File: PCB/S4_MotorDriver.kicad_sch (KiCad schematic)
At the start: 24 parts, among them J1 Motor Out, J2 ESTOP, U1 DRV8873SPWPRQ1

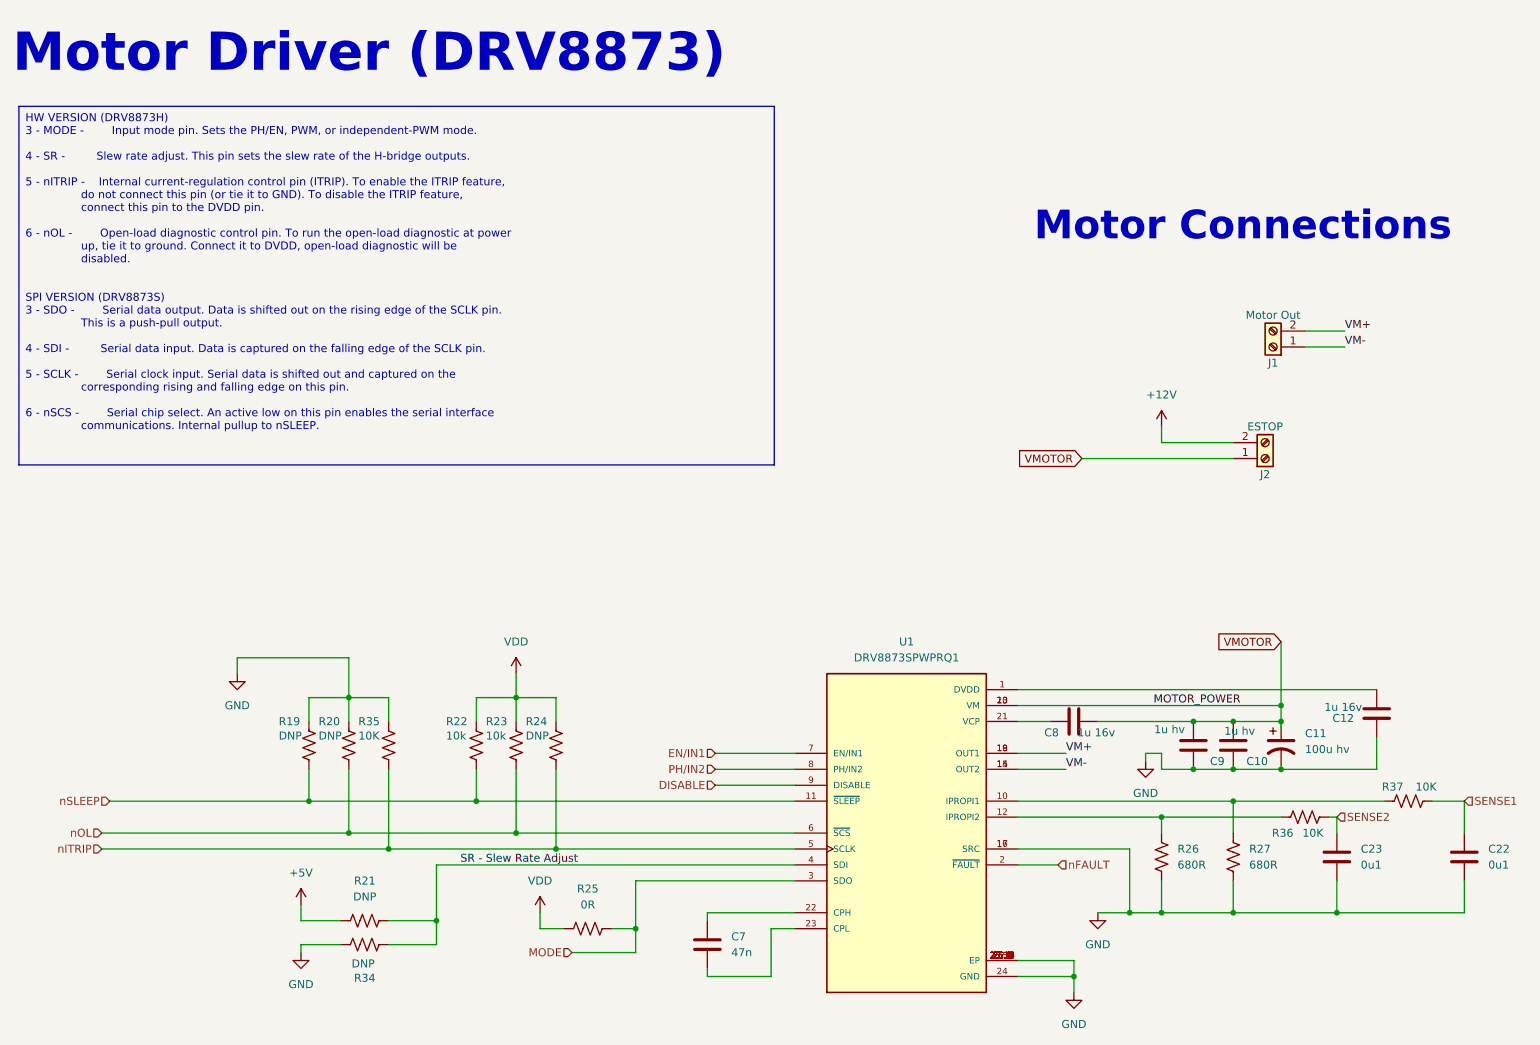
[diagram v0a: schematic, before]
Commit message: Update PCB to seperate ground symbols apporiately. Modify board to sepearte ground path for motor current and all other devices. Add filtering for slide power, hopefully reduce bownout or other issue.
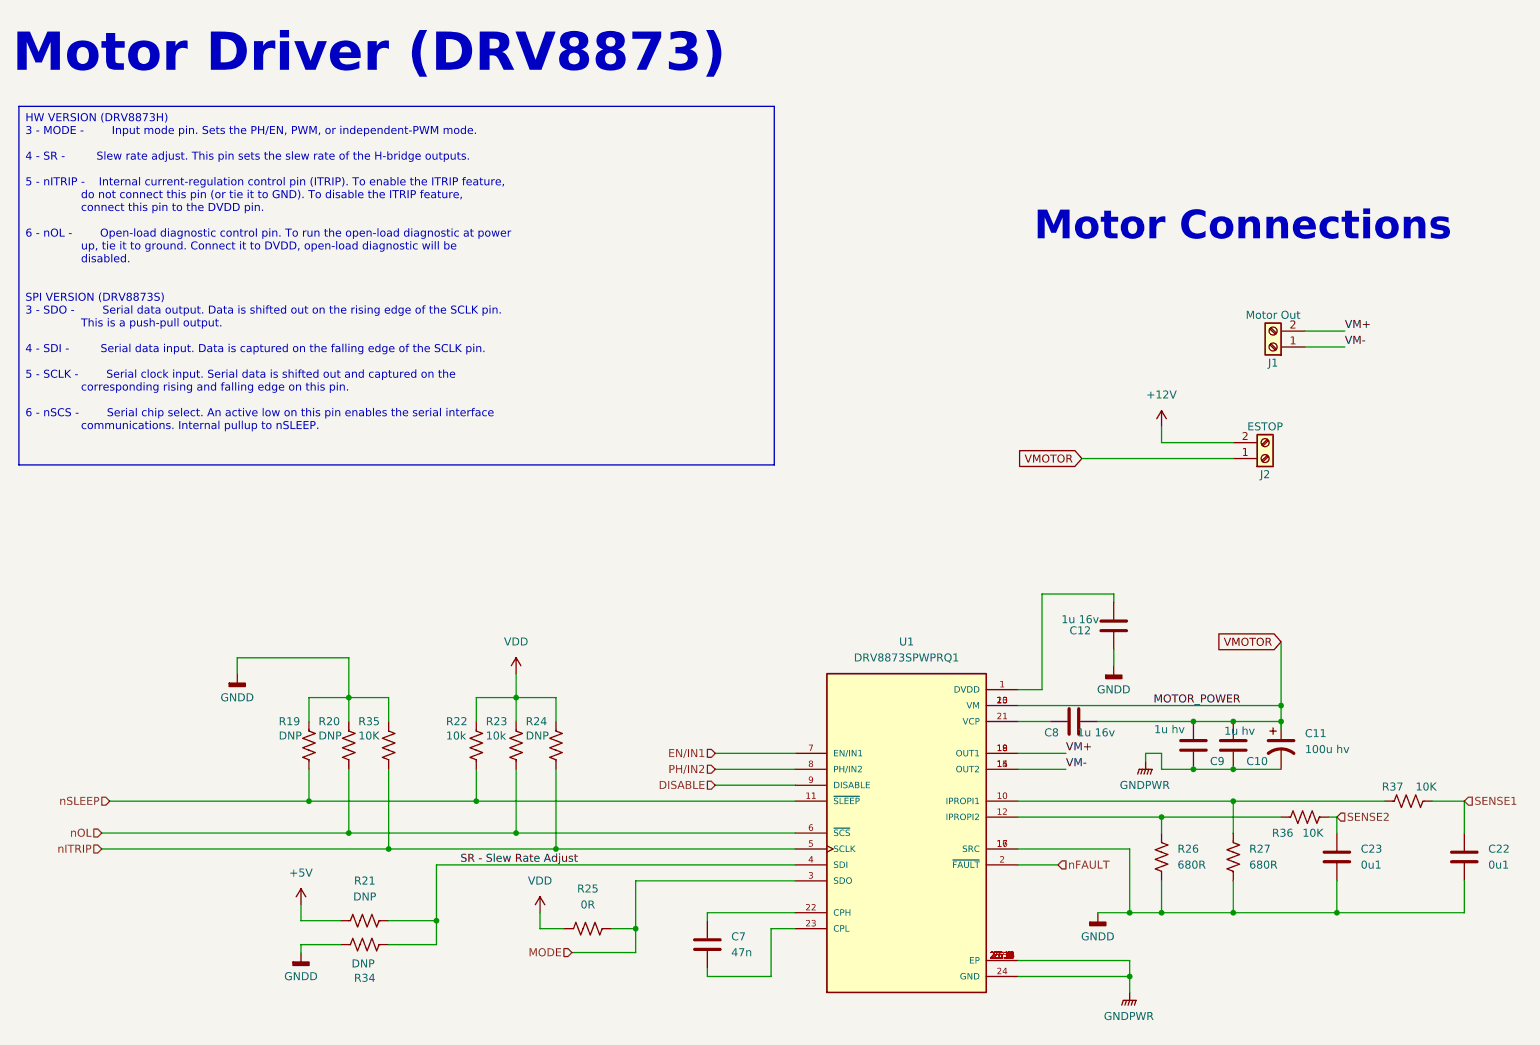
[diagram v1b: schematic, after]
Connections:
- net GND renamed GNDPWR
- net GNDPWR: no longer C12.2, C22.2, C23.2, R19.2, R20.2, R26.1, R27.1, R34.1, R35.2, U1.16 (SRC), U1.17 (SRC)
- new net GNDD: C12.2, C22.2, C23.2, R19.2, R20.2, R26.1, R27.1, R34.1, R35.2, U1.16 (SRC), U1.17 (SRC)
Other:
- moved on the sheet: C12

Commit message: WIP Adding adudino onboard, so far copying pro mega
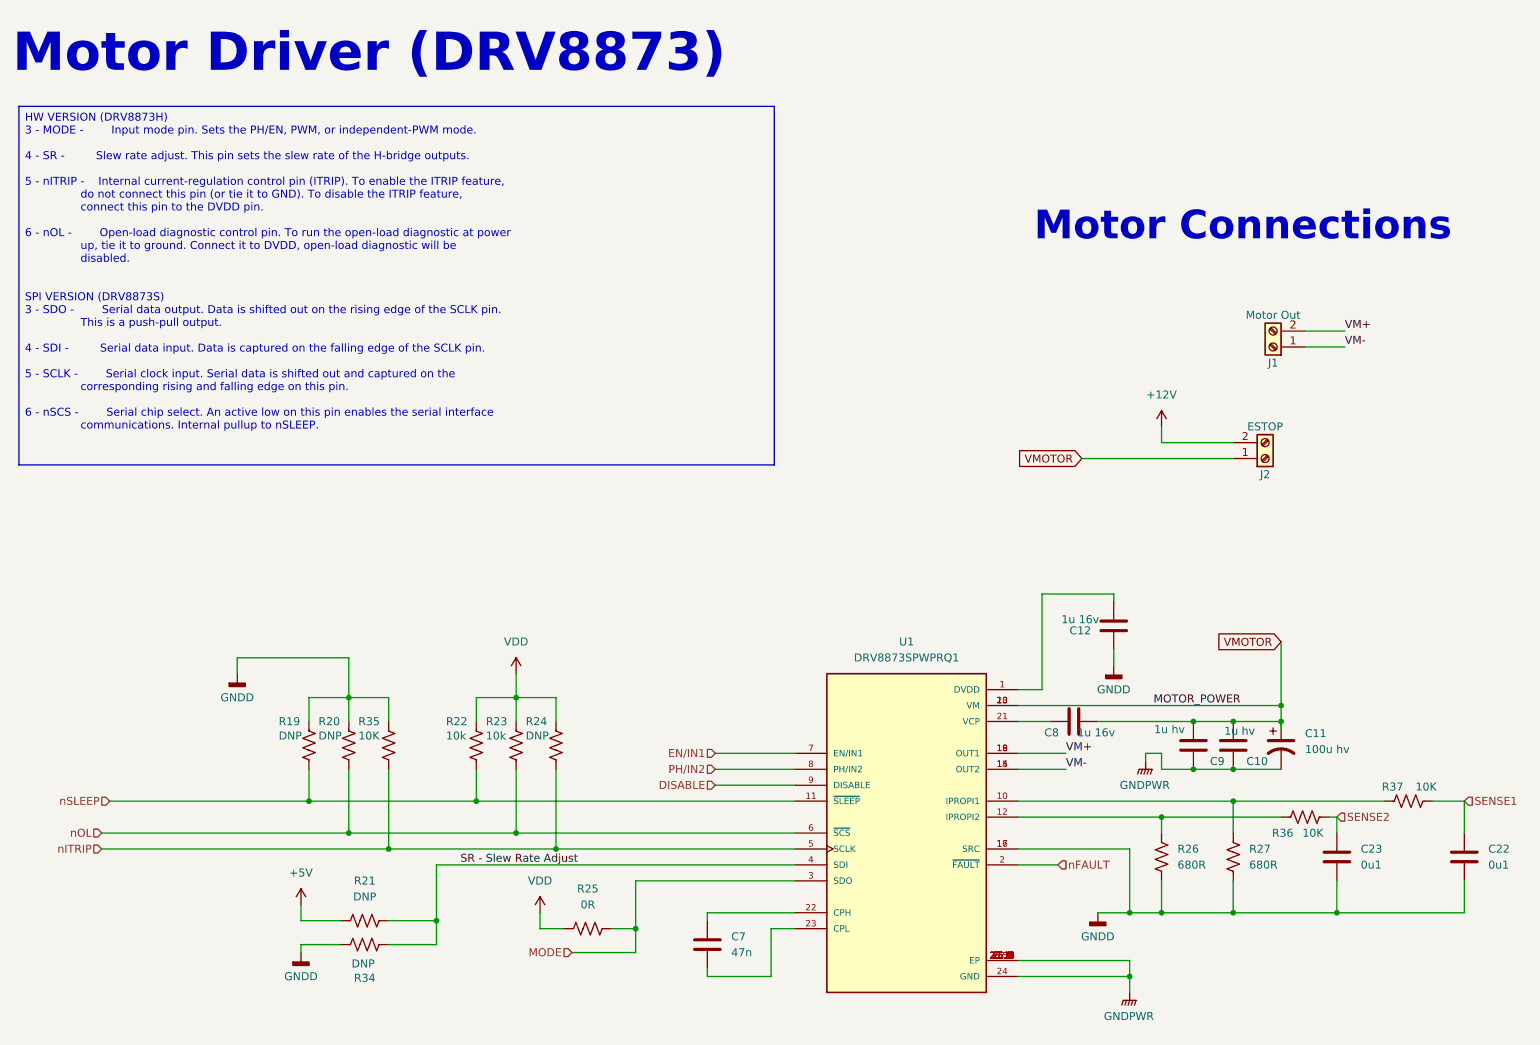
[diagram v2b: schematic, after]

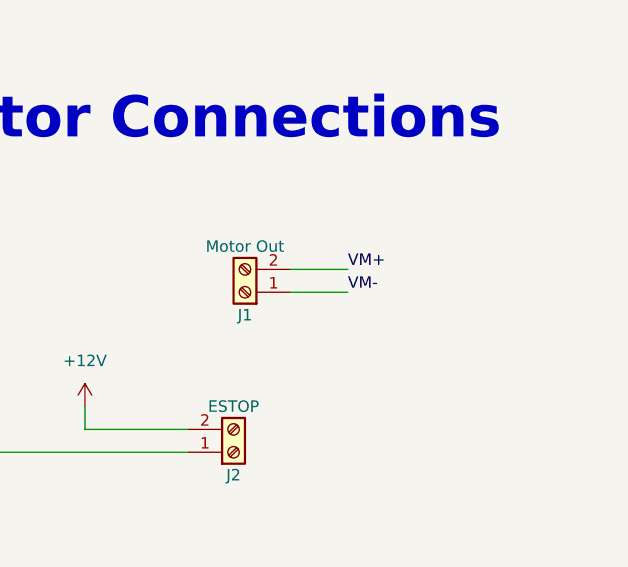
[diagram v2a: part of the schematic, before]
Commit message: Schematic bit done for adding arduino, improved motor maybe a bit by adding caps, improved slide a bit by adding protection and more caps
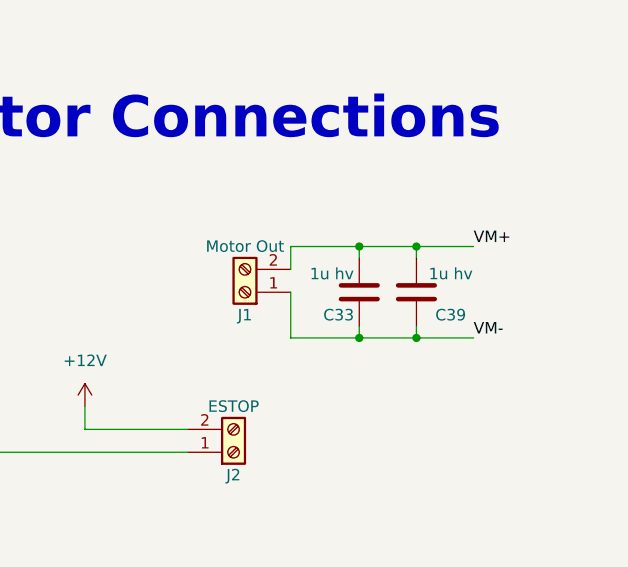
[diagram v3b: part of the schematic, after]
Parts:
- added C33, C39: 1u hv, Capacitor_SMD:C_1206_3216Metric, symbol Device:C
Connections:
- net VM+: now also C33.2, C39.2
- net VM-: now also C33.1, C39.1
